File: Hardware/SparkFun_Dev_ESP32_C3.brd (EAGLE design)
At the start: 25.4 x 25.4 mm, 88 parts, among them J1 USB Female Type C Connector, J4 QWIIC_RIGHT_ANGLE, Q1 20V/4.2A/52mΩ/1.4W, U1 ESP32-C3, U2 RT9080-33GJ5

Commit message: Shrinks design
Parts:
- removed D3: 1A/23V/620mV, SparkFun-DiscreteSemi:SOD-323
- removed H3, H4: STAND-OFF, SparkFun-Hardware:STAND-OFF
- removed LOGO2: OSHW-LOGOS, SparkFun-Aesthetics:OSHW-LOGO-S
- removed Q1: 20V/4.2A/52mΩ/1.4W, SparkFun-DiscreteSemi:SOT23-3
- removed R13, R14, R7: 100k, SparkFun-Resistors:0402-TIGHT
- removed U$1: (no value), output:#_GND#0
- removed U$11, U$12: (no value), output:ESP32#C633
- removed U$13: (no value), output:#_IO5#0
- removed U$14: (no value), output:#_IO4#0
- removed U$15: (no value), output:#_IO3#0
- removed U$16: (no value), output:#_IO2#0
- removed U$17: (no value), output:#IO16_#0
- removed U$18: (no value), output:#IO17_#0
- removed U$19: (no value), output:#IO18_#0
- removed U$2: (no value), output:#_3V3#0
- removed U$20: (no value), output:#IO19_#0
- removed U$21: (no value), output:#5_#0
- removed U$22: (no value), output:#4_#0
- removed U$25: (no value), output:QWIIC_DEV0
- removed U$3: (no value), output:#V3_#0
- removed U$31: (no value), output:#CHG#0
- removed U$32: (no value), output:CHG0
- removed U$33: (no value), output:BOOT0
- removed U$34: (no value), output:RST0
- removed U$35: (no value), output:IO90
- removed U$36: (no value), output:#VB_#0
- removed U$37: (no value), output:#_VU#0
- removed U$38: (no value), output:#3_#0
- removed U$39: (no value), output:#2_#0
- removed U$40: (no value), output:#_16#0
- removed U$41: (no value), output:#_17#0
- removed U$42: (no value), output:#_18#0
- removed U$43: (no value), output:#_19#0
- removed U$5: (no value), output:#GND_#0
- removed U$6: (no value), SparkFun-Aesthetics:SFE_LOGO_FLAME_.2
- removed U$7: (no value), output:#VU_#0
- removed U$8: (no value), output:#_VB#0
- BOOT, RESET: value MOMENTARY-SWITCH-SPST-SMD-4.6X2.8MM -> MOMENTARY-SWITCH-SPST-SMD-6.0X3.5MM; device SparkFun-Switches:TACTILE_SWITCH_SMD_4.6X2.8MM -> SparkFun-Switches:TACTILE_SWITCH_SMD_6.0X3.5MM
- J2, J3: device SparkFun-Connectors:1X06_NO_SILK -> SparkFun-Connectors:1X04_NO_SILK
- moved U1 57.7 mm to (12.7, 11.8), flipped to the bottom, turned to 180 degrees
- moved J2 26.2 mm to (1.27, 6.35), turned to 90 degrees
- moved J3 26.2 mm to (24.1, 6.35), turned to 90 degrees
- moved BOOT 14.5 mm to (20.6, 10.2), turned to 90 degrees
- moved RESET 14.2 mm to (5.08, 10.2), turned to 270 degrees
- moved FD1 11.3 mm to (17.8, 14.0)
- moved FD2 11.3 mm to (17.8, 14.0)
- moved C1 5.29 mm to (12.2, 9.65)
- moved C2 5.29 mm to (11.2, 9.65)
- moved R8 5.29 mm to (13.2, 9.65)
- moved R11 5.29 mm to (14.2, 9.65)
- moved U$23 5.11 mm to (7.62, 11.7), flipped to the bottom, turned to 180 degrees
- moved I2C 4.97 mm to (7.75, 9.91), flipped to the bottom
- moved R12 4.44 mm to (10.2, 9.65)
- moved U2 1.20 mm to (17.1, 10.4)
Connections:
- removed net IO1/V_BATT_2: R13.1, R14.2
- removed net IO18: J3.5
- removed net IO19: J3.6
- removed net IO2: J2.3
- removed net IO3: J2.4
- removed net IO4: J2.5
- removed net IO5: J2.6
- removed net N$9: C1.1, D3.C, Q1.2, R8.1, U2.1
- removed net V_BATT: J3.1, Q1.3, R13.2
- net 3.3V: no longer J2.2
- net EN: now also RESET.2; no longer RESET.3, RESET.4
- net GND: no longer BOOT.2, J2.1, R14.1, R7.1, RESET.2
- net IO20/TX: no longer J3.3
- net IO21/RX: no longer J3.4
- net IO9/BOOT: now also BOOT.2; no longer BOOT.3, BOOT.4
- net V_USB: now also C1.1, R8.1, U2.1; no longer D3.A, J3.2, Q1.1, R7.2
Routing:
- net 3.3V: track 42.4 -> 0.00 mm, vias 3 -> 0
- net V_USB: track 36.0 -> 0.00 mm, vias 3 -> 0
- net V_BATT: track 31.8 -> 0.00 mm, vias 2 -> 0
- net IO6/SDA: track 19.4 -> 0.00 mm, vias 1 -> 0
- net N$9: track 17.4 -> 0.00 mm
- net IO7/SCL: track 14.9 -> 0.00 mm, vias 1 -> 0
- net IO23/STAT: track 11.8 -> 0.00 mm, vias 2 -> 0
- net EN: track 11.2 -> 0.00 mm, vias 1 -> 0
- net IO9/BOOT: track 10.8 -> 0.00 mm, vias 1 -> 0
- net N$14: track 10.7 -> 0.00 mm, vias 1 -> 0
- net GND: track 8.34 -> 0.00 mm, vias 27 -> 0
- net IO18: track 7.22 -> 0.00 mm
- net IO19: track 6.94 -> 0.00 mm, vias 1 -> 0
- net IO5: track 6.79 -> 0.00 mm
- net IO1/V_BATT_2: track 6.57 -> 0.00 mm, vias 1 -> 0
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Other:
- board size 25.4 x 25.4 mm -> 25.4 x 15.2 mm

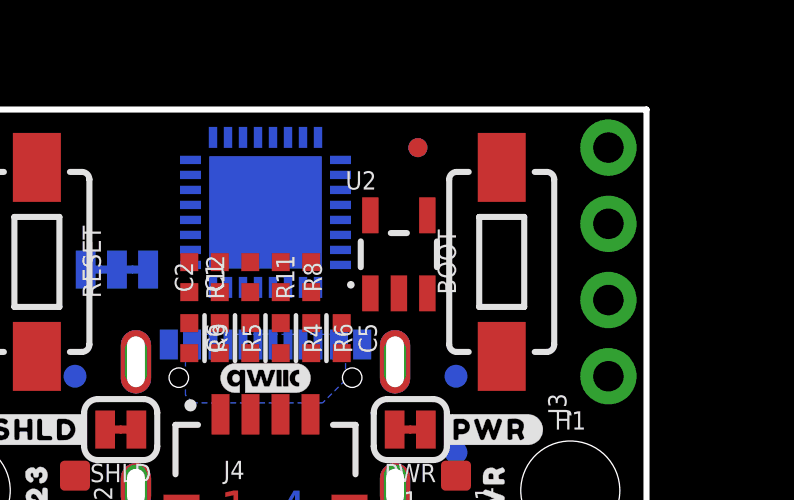
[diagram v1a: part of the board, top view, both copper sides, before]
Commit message: Adds crystal
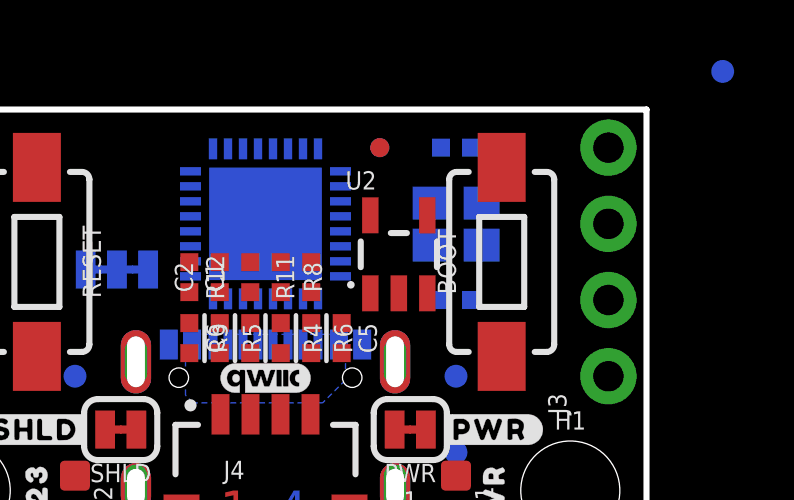
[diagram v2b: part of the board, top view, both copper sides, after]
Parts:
- added C3, C4: 9.1pF, SparkFun-Capacitors:0402-TIGHT
- added Y1: 40MHZ, SparkFun-Clocks:CRYSTAL-SMD-2X2.5MM
- moved TP4 8.52 mm to (27.9, 16.5)
- moved FD1 1.27 mm to (16.5, 14.0)
- moved FD2 1.27 mm to (16.5, 14.0)
- moved U1 0.38 mm to (12.7, 11.4), turned to 90 degrees
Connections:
- new net N$10: C4.2, U1.P30, Y1.P3
- new net N$9: C3.2, U1.P29, Y1.P1
- net GND: now also C3.1, C4.1, Y1.P2, Y1.P4
- net IO20/TX: now also J2.1
- net IO21/RX: now also J2.2

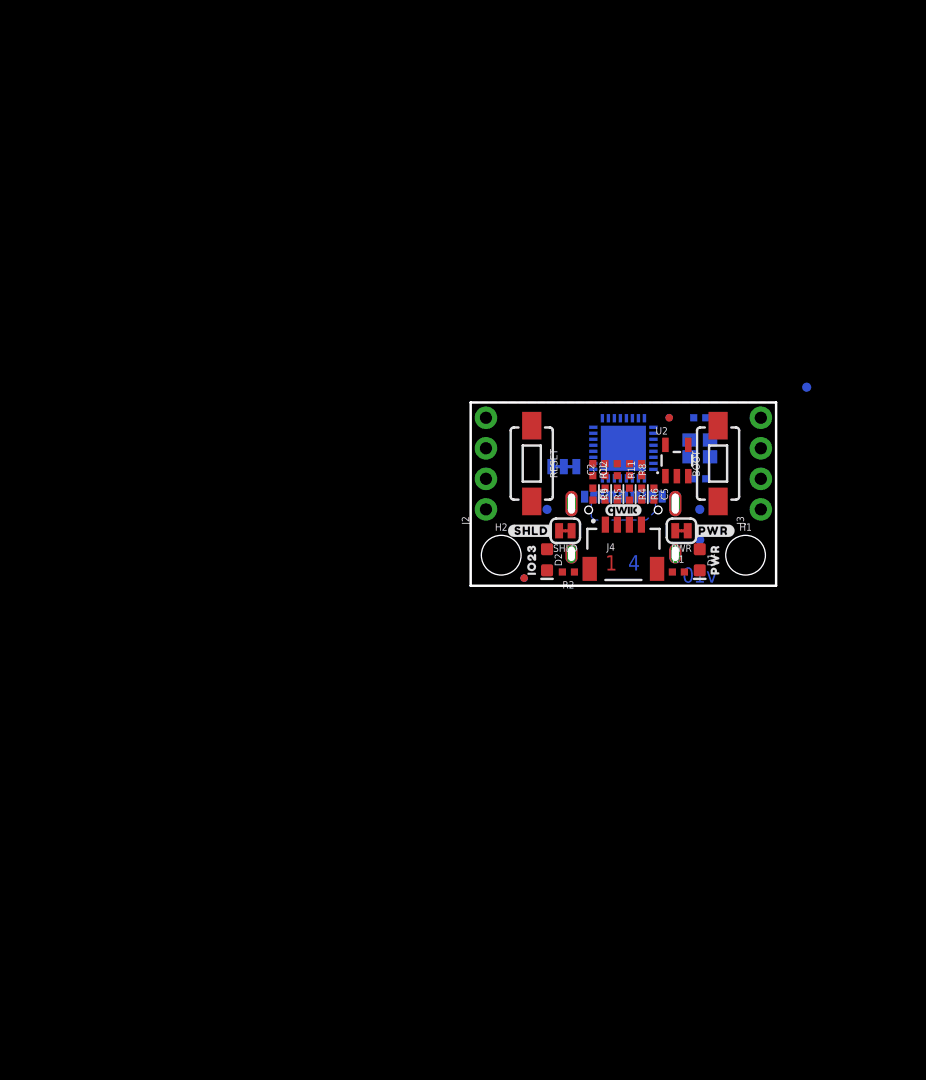
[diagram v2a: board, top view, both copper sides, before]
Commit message: Adds more documentation, decoupling caps, antennas, rearranges schematic
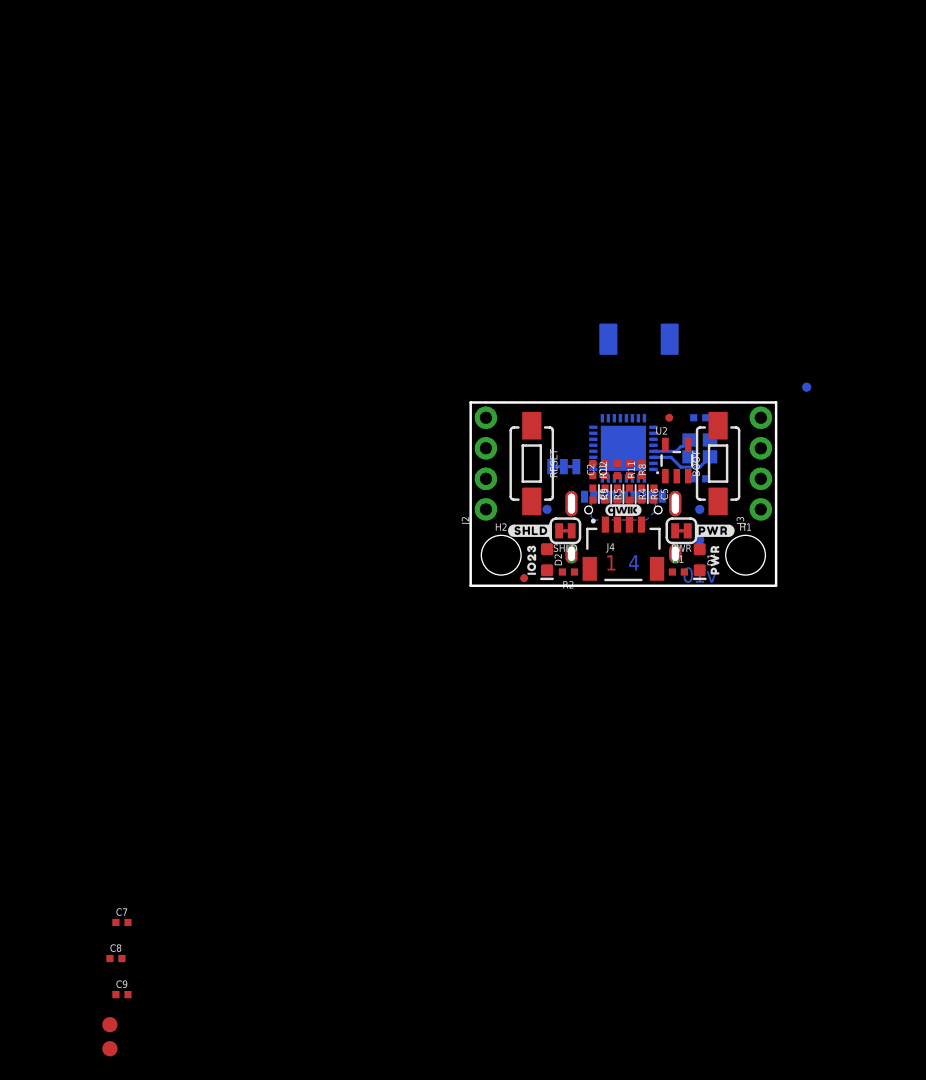
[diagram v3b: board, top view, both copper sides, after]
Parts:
- added A1: ANTENNA-2.4GHZ-FRACTUS, SparkFun-RF:ANT-2.4GHZ-7.0X3.0MM-FRACTUS
- added C7, C8: 0.1uF, SparkFun-Capacitors:0402-TIGHT
- added C9: 10nF, SparkFun-Capacitors:0402-TIGHT
- added TP5, TP6: TEST-POINT3X5, SparkFun-Connectors:PAD.03X.05
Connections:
- net 3.3V: now also C7.1, C8.1, C9.1
- net GND: now also C7.2, C8.2, C9.2, TP6.1
- net V_USB: now also TP5.1
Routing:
- net N$10: track 0.00 -> 5.40 mm
- net N$9: track 0.00 -> 3.39 mm

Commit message: Adds new antenna, nets IO, removes STAT LED
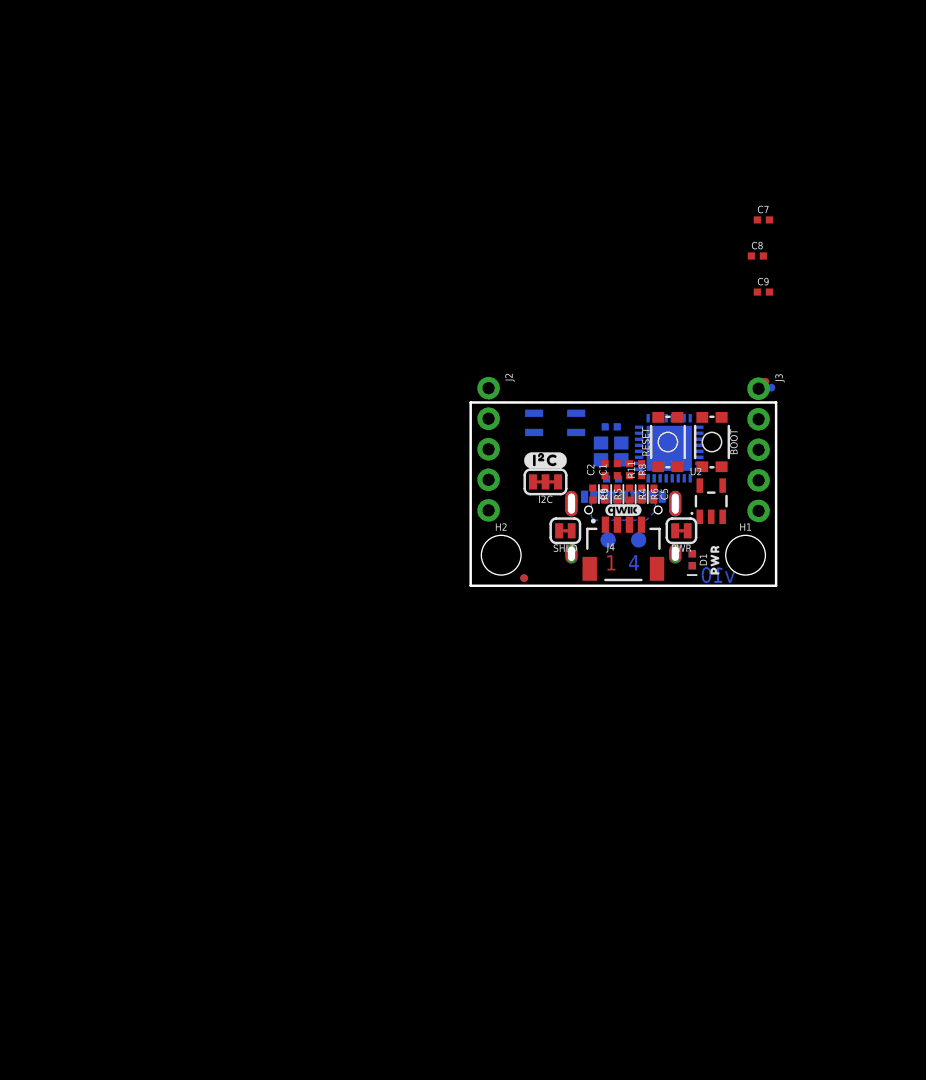
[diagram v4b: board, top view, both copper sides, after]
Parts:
- removed A1: ANTENNA-2.4GHZ-FRACTUS, SparkFun-RF:ANT-2.4GHZ-7.0X3.0MM-FRACTUS
- removed D2: BLUE, SparkFun-LED:LED-0603
- removed R12: 100k, SparkFun-Resistors:0402-TIGHT
- removed R2: 2.2k, SparkFun-Resistors:0402-TIGHT
- removed TP1, TP2, TP3, TP4: TEST-POINT3, SparkFun-Connectors:PAD.03X.03
- removed U$26: (no value), output:#PWR#0
- removed U$27: (no value), output:#SHLD#0
- removed U$28: (no value), output:IO230
- removed U$9: (no value), output:QWIIC_DEV0
- added E1: WIFI_CHIP_ANT, ESP32-C3-MINI-1:CHIP_ANT_NO_COURTYARD
- BOOT, RESET: value MOMENTARY-SWITCH-SPST-SMD-6.0X3.5MM -> MOMENTARY-SWITCH-SPST-SMD-4.6X2.8MM; device SparkFun-Switches:TACTILE_SWITCH_SMD_6.0X3.5MM -> SparkFun-Switches:TACTILE_SWITCH_SMD_4.6X2.8MM
- D1: value (none) -> RED; device SparkFun-LED:LED-0603 -> SparkFun-LED:LED-0402
- J2, J3: device SparkFun-Connectors:1X04_NO_SILK -> SparkFun-Connectors:1X05_NO_SILK
- moved C7 79.1 mm to (24.3, 30.4)
- moved C8 79.1 mm to (23.8, 27.4)
- moved C9 79.1 mm to (24.3, 24.4)
- moved TP6 61.0 mm to (14.0, 3.81), flipped to the bottom
- moved TP5 57.8 mm to (11.4, 3.81), flipped to the bottom
- moved RESET 11.5 mm to (16.4, 11.9), turned to 90 degrees
- moved J2 10.1 mm to (1.49, 16.4), turned to 270 degrees
- moved J3 10.0 mm to (23.9, 16.4), turned to 270 degrees
- moved FD1 8.86 mm to (25.0, 16.5)
- moved FD2 8.54 mm to (24.5, 17.0)
- moved C3 7.41 mm to (11.7, 13.2)
- moved Y1 7.37 mm to (11.7, 11.2)
- moved C4 7.25 mm to (11.8, 8.88)
- moved U2 4.43 mm to (20.0, 7.03)
- moved U1 3.81 mm to (16.5, 11.4), turned to 270 degrees
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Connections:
- removed net IO23/STAT: D2.A
- removed net N$14: R12.1
- removed net N$3: D2.C, R2.2
- new net IO13/SDA: R3.1, U1.P20
- new net IO14/SCL: R4.2, U1.P21
- new net IO15: J2.3, U1.P22
- new net IO3: J3.4, U1.P8
- new net IO5: J3.5, U1.P10
- new net N$11: E1.P1, U1.P1
- new net PICO: J3.2, U1.P13
- new net POCI: J3.1, U1.P6
- new net SCLK: J3.3, U1.P12
- net 3.3V: now also J2.5; no longer R12.2
- net EN: now also RESET.3, RESET.4; no longer RESET.2, TP4.1
- net GND: now also BOOT.2, E1.P3, E1.P4, J2.4, RESET.2; no longer R2.1
- net IO6/SDA: no longer R3.1, TP2.1
- net IO7/SCL: no longer R4.2, TP1.1
- net IO9/BOOT: now also BOOT.3, BOOT.4; no longer BOOT.2, TP3.1
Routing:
- net N$10: track 5.40 -> 0.00 mm
- net N$9: track 3.39 -> 0.00 mm

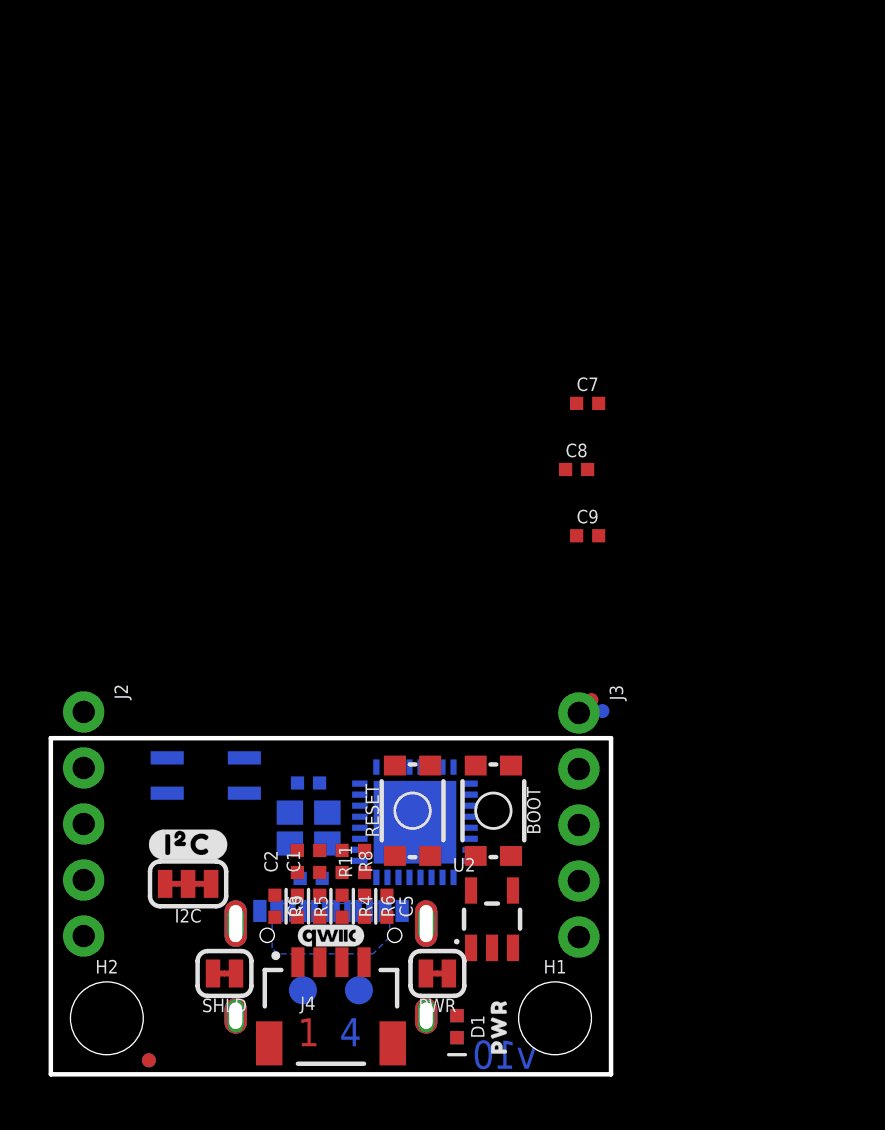
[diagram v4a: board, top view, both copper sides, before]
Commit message: Moves towards Pro Micro form factor
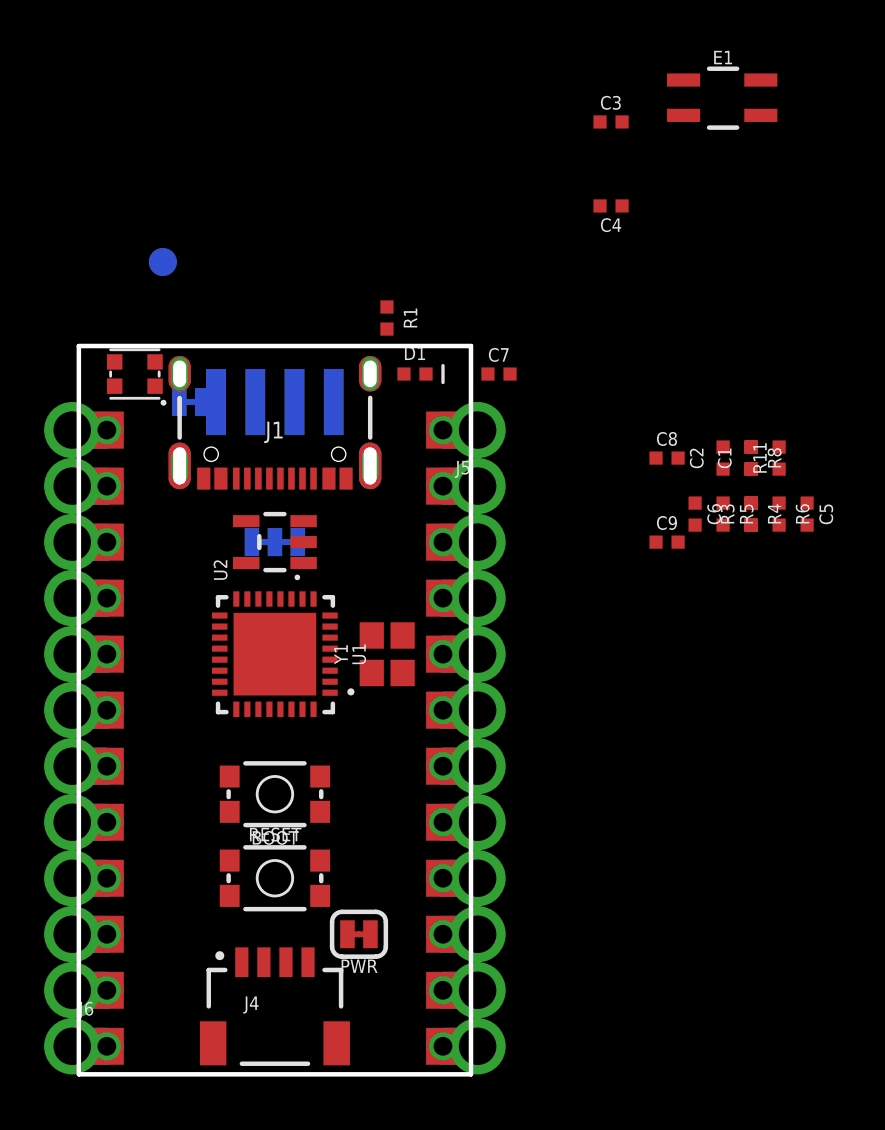
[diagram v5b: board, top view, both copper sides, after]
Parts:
- removed FD1, FD2, FD3, FD4: FIDUCIALUFIDUCIAL, SparkFun-Aesthetics:FIDUCIAL-MICRO
- removed FRAME1: FRAME-LETTER, SparkFun-Aesthetics:CREATIVE_COMMONS
- removed H1, H2: STAND-OFF, SparkFun-Hardware:STAND-OFF
- removed J2, J3: (no value), SparkFun-Connectors:1X05_NO_SILK
- removed LOGO3: QWIIC_LOGO_3MM, SparkFun-Aesthetics:QWIIC_3MM
- removed TP5, TP6: TEST-POINT3X5, SparkFun-Connectors:PAD.03X.05
- removed U$10: (no value), SparkFun-Aesthetics:SFE_LOGO_FLAME_.1
- removed U$23: (no value), output:#I�C#0
- removed U$30: (no value), output:PWR0
- added FRAME2: FRAME-LEDGER, SparkFun-Aesthetics:CREATIVE_COMMONS
- added J5, J6: (no value), Castellated:1X12_CASTELLATED
- added JP14: USB_SOLDER_PADS, SparkFun-Connectors:USB-SOLDER-PADS
- added TP3: (no value), SparkFun-Connectors:PAD.03X.05
- added U3: WS2812-2020, SparkFun-LED:WS2812-2020
- moved E1 38.7 mm to (30.5, 44.5), flipped to the top
- moved C4 33.4 mm to (25.4, 39.4), flipped to the top
- moved C3 33.0 mm to (25.4, 43.2), flipped to the top
- moved R1 32.3 mm to (15.2, 34.3), flipped to the top
- moved D1 29.7 mm to (16.5, 31.8), turned to 0 degrees
- moved C1 26.8 mm to (31.8, 27.9)
- moved C2 26.6 mm to (30.5, 27.9)
- moved R3 26.4 mm to (31.8, 25.4)
- moved R5 26.2 mm to (30.5, 25.4)
- moved R11 26.2 mm to (33.0, 27.9)
- moved C5 26.1 mm to (34.3, 25.4)
- moved C6 26.1 mm to (29.2, 25.4)
- moved R8 26.0 mm to (31.8, 27.9)
- moved SHLD 26.0 mm to (6.35, 30.5), flipped to the bottom
- moved R6 25.9 mm to (33.0, 25.4)
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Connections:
- new net !RESET!: J6.3, J6.3B
- new net 0/TX0: J5.12, J5.12B
- new net 1/RX0: J5.11, J5.11B
- new net 2: J5.8, J5.8B
- new net 20/SPI_CIPO: J6.10, J6.10B
- new net 21/SPI_!CS!: J6.12, J6.12B
- new net 22/SPI_SCK: J6.9, J6.9B
- new net 23/SPI_COPI: J6.11, J6.11B
- new net 25/WS2812-DI: U3.3
- new net 3: J5.7, J5.7B
- new net 4: J5.6, J5.6B
- new net 5: J5.5, J5.5B
- new net 6: J5.4, J5.4B
- new net 7: J5.3, J5.3B
- new net 8/TX1: J5.2, J5.2B
- new net 9/RX1: J5.1, J5.1B
- new net A0: J6.8, J6.8B
- new net A1: J6.7, J6.7B
- new net A2: J6.6, J6.6B
- new net A3: J6.5, J6.5B
- new net GND1: JP14.GND
- new net N$3: TP3.P$1, U3.1
- new net RAW: J6.1, J6.1B, U3.4
- new net RP_D+: JP14.D+
- new net RP_D-: JP14.D-
- net 3.3V: now also J6.4, J6.4B; no longer J2.5
- net GND: now also J5.10, J5.10B, J5.9, J5.9B, J6.2, J6.2B, U3.2; no longer J2.4, TP6.1
- net IO15: no longer J2.3
- net IO20/TX: no longer J2.1
- net IO21/RX: no longer J2.2
- net IO3: no longer J3.4
- net IO5: no longer J3.5
- net PICO: no longer J3.2
- net POCI: no longer J3.1
- net SCLK: no longer J3.3
- net V_USB: now also JP14.VBUS; no longer TP5.1
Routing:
- removed copper zone on layer 1, net GND
- removed copper zone on layer 16, net GND
- removed copper zone on layer 16, net V_USB
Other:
- board size 25.4 x 15.2 mm -> 17.8 x 33 mm
- board text removed: "1"
- board text removed: "4"
- board text removed: "v10"
